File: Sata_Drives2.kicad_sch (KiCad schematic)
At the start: 66 parts

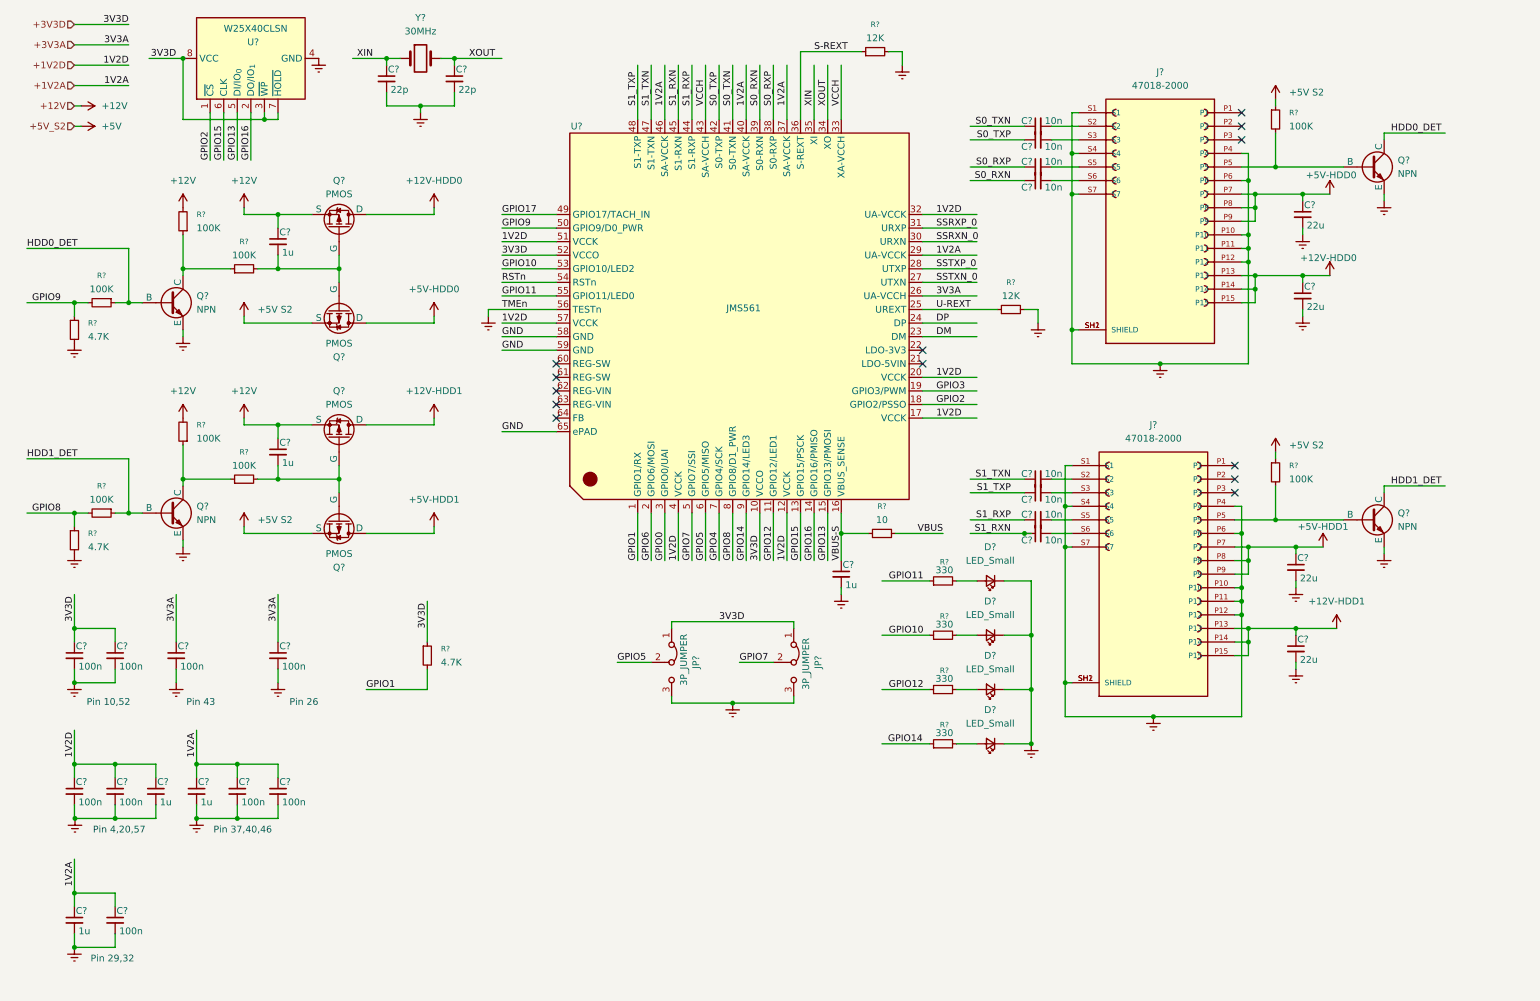
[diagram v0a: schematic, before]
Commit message: Swiitched to JSM561
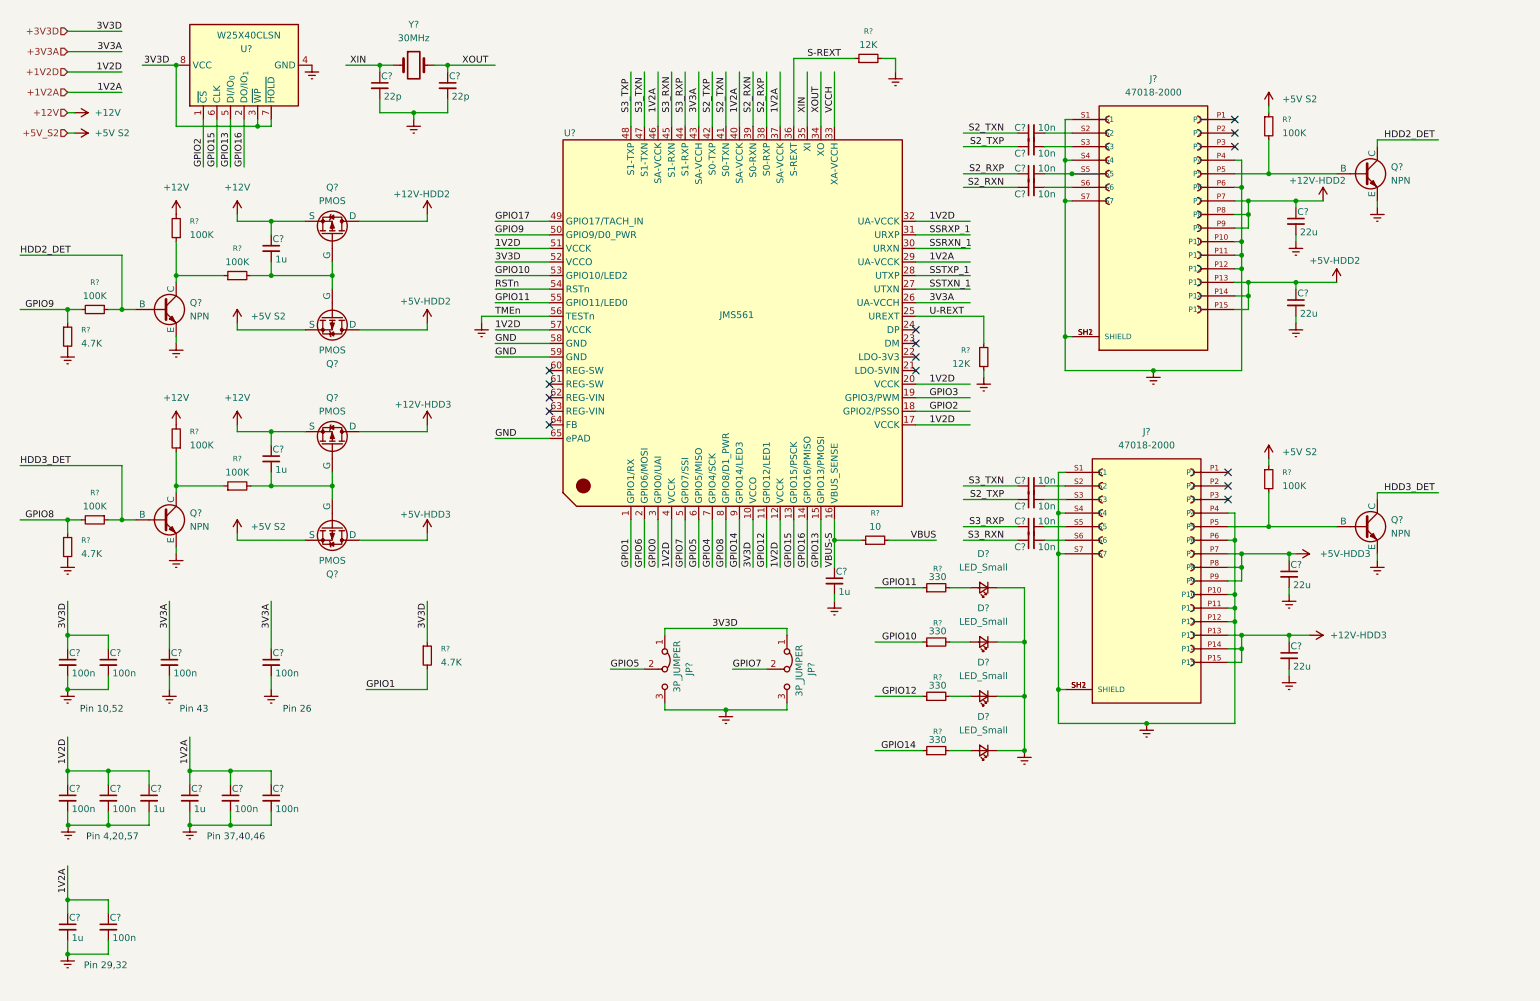
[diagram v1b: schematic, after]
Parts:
- removed C? (x9): 100n, symbol Device:C_Small
- removed C? (x4): 22u, symbol Device:C_Small
- removed C? (x8): 10n, symbol Device:C_Small
- removed C? (x6): 1u, symbol Device:C_Small
- removed C? (x2): 22p, symbol Device:C_Small
- removed D? (x4): LED_Small, symbol Device:LED_Small
- removed J? (x2): 47018-2000, 47018-2000:MOLEX_47018-2000, symbol 47018-2000:47018-2000
- removed JP? (x2): 3P_JUMPER, symbol Jumper:Jumper_3_Bridged12
- removed Q? (x4): PMOS, symbol Simulation_SPICE:PMOS
- removed Q? (x4): NPN, symbol Simulation_SPICE:NPN
- removed R? (x3): 4.7K, symbol Device:R_Small
- removed R? (x8): 100K, symbol Device:R_Small
- removed R? (x4): 330, symbol Device:R_Small
- removed R?: 10, symbol Device:R_Small
- removed R? (x2): 12K, symbol Device:R_Small
- removed U?: JMS561, Package_DFN_QFN:QFN-64-1EP_8x8mm_P0.4mm_EP6.5x6.5mm, symbol JMS561:JMS561
- removed U?: W25X40CLSN, Package_SO:SOIC-8_3.9x4.9mm_P1.27mm, symbol Memory_Flash:W25X40CLSN
- removed Y?: 30MHz, symbol Device:Crystal
- added C? (x4): 22u, symbol Device:C_Small
- added C? (x2): 22p, symbol Device:C_Small
- added C? (x9): 100n, symbol Device:C_Small
- added C? (x6): 1u, symbol Device:C_Small
- added C? (x8): 10n, symbol Device:C_Small
- added D? (x4): LED_Small, symbol Device:LED_Small
- added J? (x2): 47018-2000, 47018-2000:MOLEX_47018-2000, symbol 47018-2000:47018-2000
- added JP? (x2): 3P_JUMPER, symbol Jumper:Jumper_3_Bridged12
- added Q? (x4): NPN, symbol Simulation_SPICE:NPN
- added Q? (x4): PMOS, symbol Simulation_SPICE:PMOS
- added R? (x8): 100K, symbol Device:R_Small
- added R? (x4): 330, symbol Device:R_Small
- added R? (x3): 4.7K, symbol Device:R_Small
- added R?: 10, symbol Device:R_Small
- added R? (x2): 12K, symbol Device:R_Small
- added U?: JMS561, Package_DFN_QFN:QFN-64-1EP_8x8mm_P0.4mm_EP6.5x6.5mm, symbol JMS561:JMS561
- added U?: W25X40CLSN, Package_SO:SOIC-8_3.9x4.9mm_P1.27mm, symbol Memory_Flash:W25X40CLSN
- added Y?: 30MHz, symbol Device:Crystal
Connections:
- net +12V: now also C?.1, C?.1, Q?.3 (S), Q?.3 (S), R?.2, R?.2
- net +1V2A: now also C?.1, C?.1, C?.1, C?.1, C?.1, U?.29 (UA-VCCK), U?.37 (SA-VCCK), U?.40 (SA-VCCK), U?.46 (SA-VCCK)
- net +1V2D: now also C?.1, C?.1, C?.1, U?.12 (VCCK), U?.17 (VCCK), U?.20 (VCCK), U?.32 (UA-VCCK), U?.4 (VCCK), U?.51 (VCCK), U?.57 (VCCK)
- net +3V3A: now also C?.1, C?.1, U?.26 (UA-VCCH), U?.43 (SA-VCCH)
- net +3V3D: now also C?.1, C?.1, JP?.1 (A), JP?.1 (A), R?.1, U?.10 (VCCO), U?.3 (~{WP}), U?.52 (VCCO), U?.7 (~{HOLD}), U?.8 (VCC)
- net +5V S2: now also Q?.3 (S), Q?.3 (S), R?.1, R?.1
- net GND: now also U?.58 (GND), U?.59 (GND), U?.65 (ePAD)
- net GPIO0: now also U?.3 (GPIO0/UAI)
- net GPIO1: now also R?.2, U?.1 (GPIO1/RX)
- net GPIO10: now also R?.1, U?.53 (GPIO10/LED2)
- net GPIO11: now also R?.1, U?.55 (GPIO11/LED0)
- net GPIO12: now also R?.1, U?.11 (GPIO12/LED1)
- net GPIO13: now also U?.15 (GPIO13/PMOSI), U?.5 (DI/IO_{0})
- net GPIO14: now also R?.1, U?.9 (GPIO14/LED3)
- net GPIO15: now also U?.13 (GPIO15/PSCK), U?.6 (CLK)
- net GPIO16: now also U?.14 (GPIO16/PMISO), U?.2 (DO/IO_{1})
- net GPIO17: now also U?.49 (GPIO17/TACH_IN)
- net GPIO2: now also U?.1 (~{CS}), U?.18 (GPIO2/PSSO)
- net GPIO3: now also U?.19 (GPIO3/PWM)
- net GPIO4: now also U?.7 (GPIO4/SCK)
- net GPIO5: now also JP?.2 (C), U?.6 (GPIO5/MISO)
- net GPIO6: now also U?.2 (GPIO6/MOSI)
- net GPIO7: now also JP?.2 (C), U?.5 (GPIO7/SSI)
- net GPIO8: now also R?.1, R?.2, U?.8 (GPIO8/D1_PWR)
- net GPIO9: now also R?.1, R?.2, U?.50 (GPIO9/D0_PWR)
- net RSTn: now also U?.54 (RSTn)
- net S-REXT: now also R?.1, U?.36 (S-REXT)
- net TMEn: now also U?.56 (TESTn)
- net U-REXT: now also R?.2, U?.25 (UREXT)
- net VBUS: now also R?.2
- net VBUS-S: now also C?.1, R?.1, U?.16 (VBUS_SENSE)
- net VCCH: now also U?.33 (XA-VCCH)
- net XIN: now also C?.1, U?.35 (XI), Y?.1
- net XOUT: now also C?.1, U?.34 (XO), Y?.2
- new net: J?.P5, Q?.2 (B), R?.2 (x2)
- new net: Q?.1 (C), R?.1, R?.1 (x2)
- new net: C?.2, Q?.2 (G), Q?.2 (G), R?.2 (x2)
- new net: D?.1 (K), D?.1 (K), D?.1 (K), D?.1 (K)
- new net: D?.2 (A), R?.2 (x4)
- new net: C?.2, C?.2 (x3)
- new net: C?.2, C?.2, C?.2 (x2)
- new net: C?.2, J?.S2 (x2)
- new net: C?.2, J?.S6 (x2)
- new net: C?.2, J?.S3 (x2)
- new net: J?.P10, J?.P11, J?.P12, J?.P4, J?.P6, J?.S1, J?.S4, J?.S7, J?.SH1 (SHIELD), J?.SH2 (SHIELD) (x2)
- new net: C?.2, J?.S5 (x2)
- new net: JP?.3 (B), JP?.3 (B)
- new net +12V-HDD2: C?.1, J?.P7, J?.P8, J?.P9, Q?.1 (D)
- new net +12V-HDD3: C?.1, J?.P13, J?.P14, J?.P15, Q?.1 (D)
- new net +5V-HDD2: C?.1, J?.P13, J?.P14, J?.P15, Q?.1 (D)
- new net +5V-HDD3: C?.1, J?.P7, J?.P8, J?.P9, Q?.1 (D)
- new net HDD2_DET: Q?.1 (C), Q?.2 (B), R?.1
- new net HDD3_DET: Q?.1 (C), Q?.2 (B), R?.1
- new net S2_RXN: C?.1, U?.39 (S0-RXN)
- new net S2_RXP: C?.1, U?.38 (S0-RXP)
- new net S2_TXN: C?.1, U?.41 (S0-TXN)
- new net S2_TXP: C?.1, C?.1, U?.42 (S0-TXP)
- new net S3_RXN: C?.1, U?.45 (S1-RXN)
- new net S3_RXP: C?.1, U?.44 (S1-RXP)
- new net S3_TXN: C?.1, U?.47 (S1-TXN)
- new net S3_TXP: U?.48 (S1-TXP)
- new net SSRXN_1: U?.30 (URXN)
- new net SSRXP_1: U?.31 (URXP)
- new net SSTXN_1: U?.27 (UTXN)
- new net SSTXP_1: U?.28 (UTXP)
- no-connect marks 13 -> 15

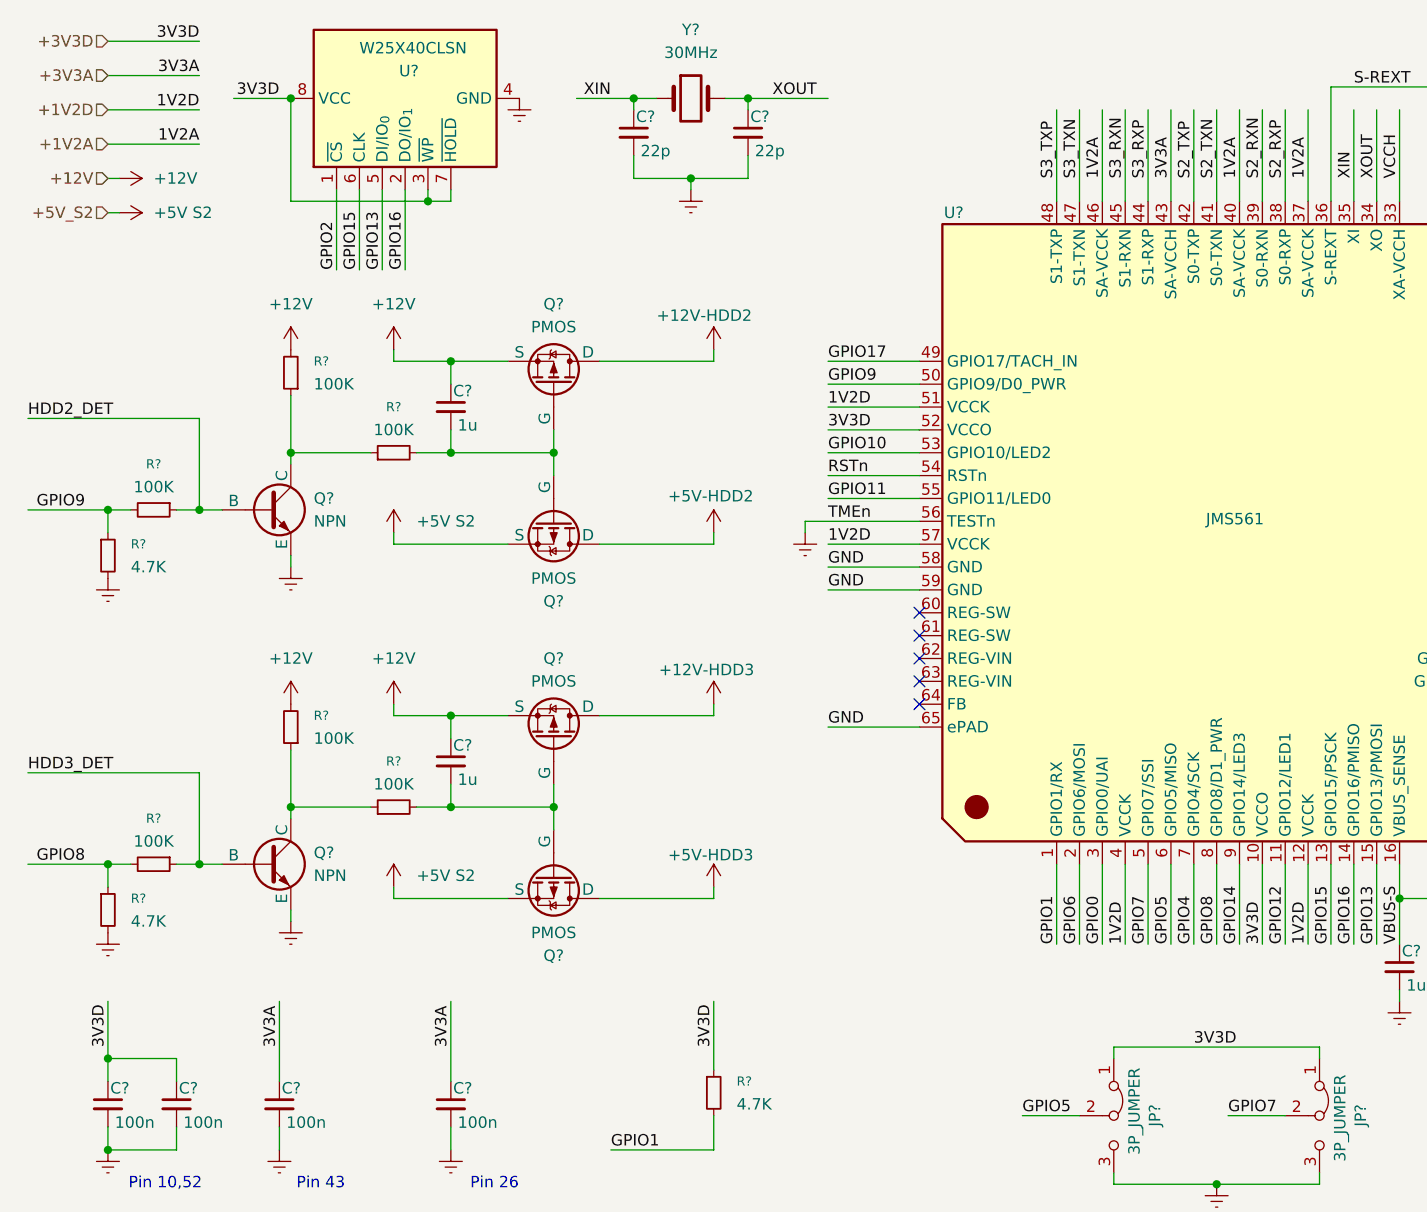
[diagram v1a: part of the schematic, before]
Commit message: Removed Ethernet
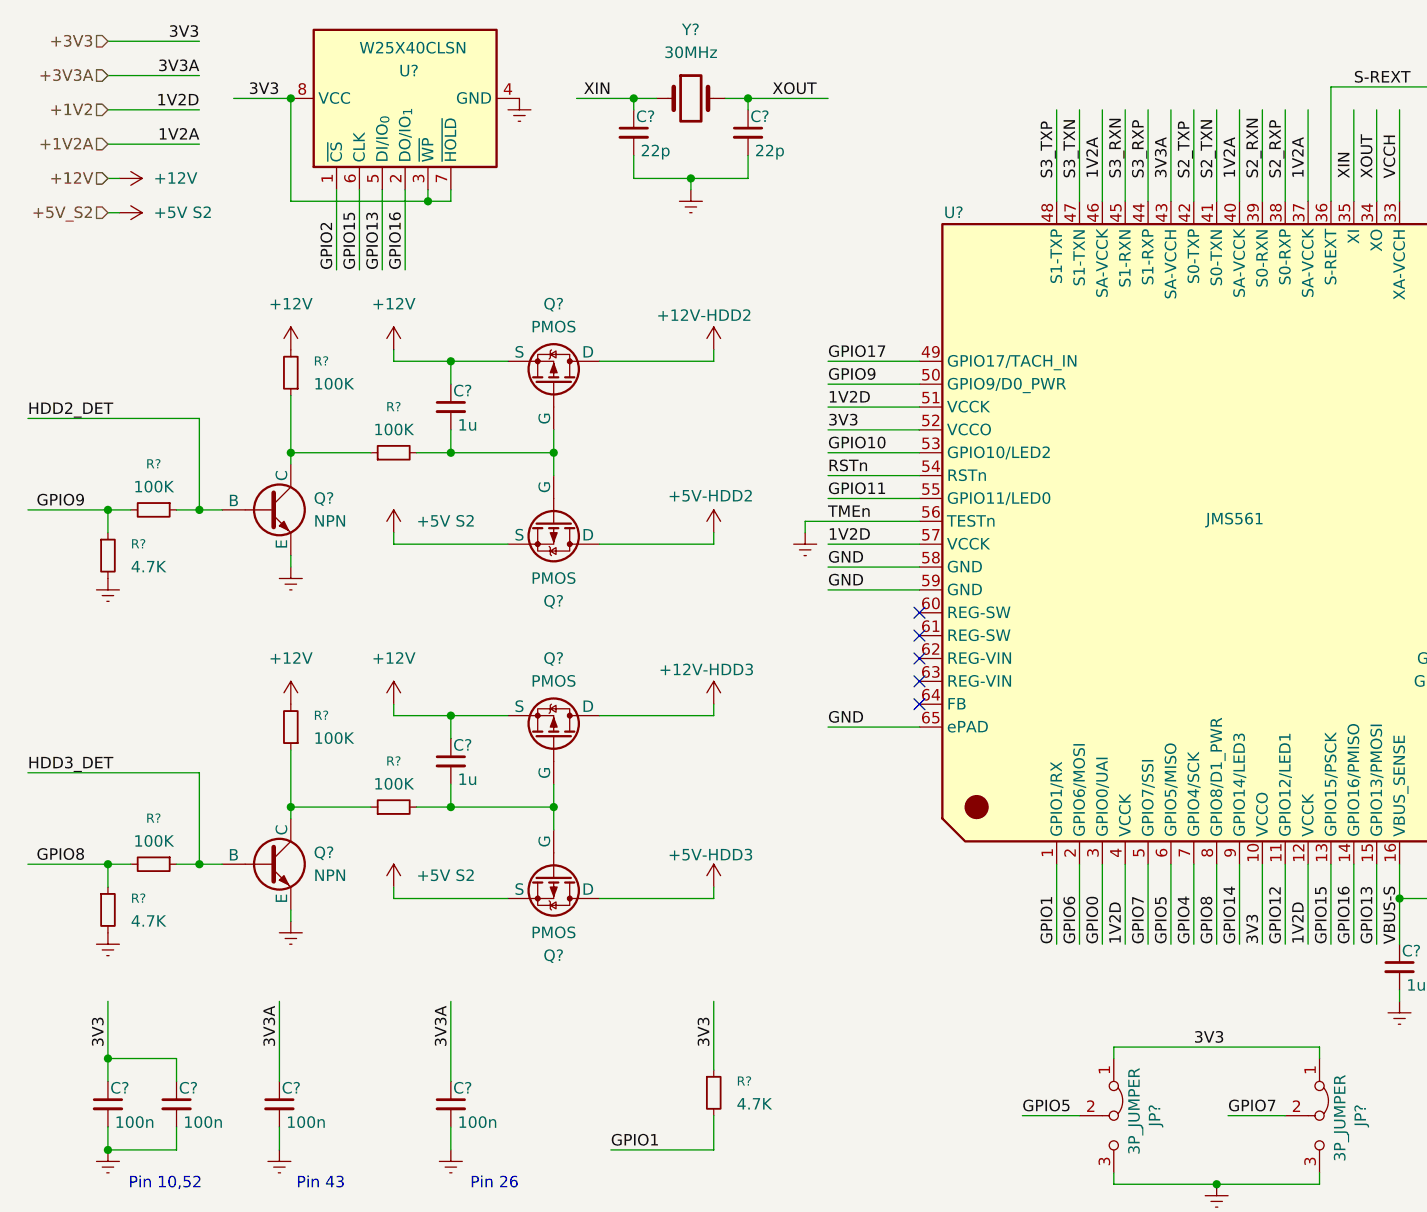
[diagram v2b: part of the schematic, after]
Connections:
- net +1V2D renamed +1V2
- net +3V3D renamed +3V3
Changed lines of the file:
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@@
 		)
 	)
-	(label "3V3D"
+	(label "3V3"
 		(at 151.13 116.84 90)
 		(effects
@@
 		)
 	)
-	(label "3V3D"
+	(label "3V3"
 		(at 90.17 128.27 90)
 		(effects
@@
 		)
 	)
-	(label "3V3D"
+	(label "3V3"
 		(at 41.91 22.86 180)
 		(effects
@@
 		)
 	)
-	(label "3V3D"
+	(label "3V3"
 		(at 33.02 16.51 180)
 		(effects
@@
 		)
 	)
-	(label "3V3D"
+	(label "3V3"
 		(at 22.86 128.27 90)
 		(effects
@@
 		)
 	)
-	(label "3V3D"
+	(label "3V3"
 		(at 102.87 59.69 0)
 		(effects
@@
 		)
 	)
-	(label "3V3D"
+	(label "3V3"
 		(at 143.51 128.27 0)
 		(effects
@@
 		)
 	)
-	(hierarchical_label "+3V3D"
+	(hierarchical_label "+3V3"
 		(shape input)
 		(at 22.86 16.51 180)
@@
 		)
 	)
-	(hierarchical_label "+1V2D"
+	(hierarchical_label "+1V2"
 		(shape input)
 		(at 22.86 24.13 180)
